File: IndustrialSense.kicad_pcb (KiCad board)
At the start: 6 copper layers, 0 parts

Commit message: [PCB/SCH][Added] Preliminary version
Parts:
- added C1: 47uF, easyeda2kicad:CAP-SMD_BD6.3-L6.6-W6.6-LS7.6-FD, F.Cu at (92.0, 112.7)
- added C12: 100n, Capacitor_SMD:C_0603_1608Metric, F.Cu at (105.7, 87.9)
- added C13: 22u, Capacitor_SMD:C_0805_2012Metric, F.Cu at (122.6, 93.0)
- added C14: 10u, Capacitor_SMD:C_1210_3225Metric, F.Cu at (120.5, 98.1)
- added C15: 100n, Capacitor_SMD:C_0402_1005Metric, F.Cu at (117.0, 96.9)
- added C16: 3.3n, Capacitor_SMD:C_0603_1608Metric, F.Cu at (115.0, 94.4)
- added C17: 100n, Capacitor_SMD:C_0402_1005Metric, F.Cu at (101.1, 121.6)
- added C18: 100n, Capacitor_SMD:C_0402_1005Metric, F.Cu at (89.8, 119.0)
- added C19: 100n, Capacitor_SMD:C_0402_1005Metric, F.Cu at (114.8, 112.4)
- added C20: 100n, Capacitor_SMD:C_0402_1005Metric, F.Cu at (112.3, 106.3)
- added C21: 10u, Capacitor_SMD:C_1210_3225Metric, F.Cu at (90.8, 107.3)
- added C22: 100n, Capacitor_SMD:C_0402_1005Metric, F.Cu at (90.7, 104.8)
- added C23: 10u, Capacitor_SMD:C_1210_3225Metric, F.Cu at (125.0, 123.8)
- added C24: 100n, Capacitor_SMD:C_0402_1005Metric, F.Cu at (95.4, 106.3)
- added C25: 220n, Capacitor_SMD:C_0402_1005Metric, F.Cu at (103.4, 107.2)
- added C26: 100n, Capacitor_SMD:C_0603_1608Metric, F.Cu at (104.2, 87.9)
- added C37: 1u, Capacitor_SMD:C_0402_1005Metric, F.Cu at (112.6, 122.1)
- added C38: 1u, Capacitor_SMD:C_0402_1005Metric, F.Cu at (135.1, 122.2)
- added C39: 1u, Capacitor_SMD:C_0402_1005Metric, F.Cu at (131.3, 122.2)
- added C4: 100u, Capacitor_SMD:C_1210_3225Metric, F.Cu at (117.5, 105.1)
- added C40: 100n, Capacitor_SMD:C_0603_1608Metric, F.Cu at (97.3, 58.3)
- added C41: 10u, Capacitor_SMD:C_0603_1608Metric, F.Cu at (95.8, 58.3)
- added C42: 10u, Capacitor_SMD:C_0603_1608Metric, F.Cu at (145.3, 64.3)
- added C43: 100n, Capacitor_SMD:C_0603_1608Metric, F.Cu at (143.8, 64.3)
- added C44: 100n, Capacitor_SMD:C_0402_1005Metric, F.Cu at (132.6, 83.4)
- added C45: 10u, Capacitor_SMD:C_0402_1005Metric, F.Cu at (133.6, 83.4)
- added C46: 1u, Capacitor_SMD:C_0603_1608Metric, F.Cu at (123.1, 82.5)
- added C47: 1u, Capacitor_SMD:C_0603_1608Metric, F.Cu at (118.9, 85.7)
- added C48: 100n, Capacitor_SMD:C_0603_1608Metric, F.Cu at (123.1, 84.0)
- added C5: 100n, Capacitor_SMD:C_0402_1005Metric, F.Cu at (130.1, 124.3)
- added C6: 100u, Capacitor_SMD:C_1210_3225Metric, F.Cu at (117.5, 101.8)
- added C7: 10u, easyeda2kicad:CAP-SMD_BD6.3-L6.6-W6.6-LS7.6-FD, F.Cu at (124.6, 116.6)
- added CN1: BM04B-SRSS-TB(LF)(SN), easyeda2kicad:CONN-SMD_BM04B-SRSS-TB, F.Cu at (92.3, 74.5)
- added CN2: B4B-ZR (LF)(SN), easyeda2kicad:CONN-TH_B4B-ZR-LF-SN, F.Cu at (92.1, 83.0)
- added CN3: ZH1.5-6P-LT, easyeda2kicad:CONN-SMD_ZH1.5-6P-LT, F.Cu at (125.8, 130.6)
- added Card1: XKTF-0803-0, easyeda2kicad:TF-SMD_XKTF-0803-0, F.Cu at (141.4, 84.6)
- added D1: SS24, Diode_SMD:D_SMA, F.Cu at (97.1, 90.2)
- added D10: CDSOT23-SM712, easyeda2kicad:SOT-23_L2.9-W1.3-P1.90-LS2.4-BR, F.Cu at (96.4, 83.1)
- added D16: WHITE2, LED_SMD:LED_0603_1608Metric, F.Cu at (98.3, 110.5)
- added D2: SS24, Diode_SMD:D_SMA, F.Cu at (91.6, 92.1)
- added D3: PESD0402-140, easyeda2kicad:D0402-BI, F.Cu at (143.4, 68.6)
- added D4: BV24C, easyeda2kicad:SOD-323_L1.7-W1.3-LS2.6-BI, F.Cu at (110.7, 123.6)
- added D5: DT1042-04SO-7, easyeda2kicad:SOT-26_L3.0-W1.6-P0.95-LS2.8-BL, F.Cu at (106.3, 121.7)
- added D6: 1N5819WS, Diode_SMD:D_SOD-323, F.Cu at (129.7, 88.5)
- added D7: 1N5819WS, Diode_SMD:D_SOD-323, F.Cu at (129.7, 91.4)
- added D8: 1N5819WS, Diode_SMD:D_SOD-323, F.Cu at (129.7, 94.3)
- added J2: Conn_02x05_Odd_Even, Connector_PinHeader_2.54mm:PinHeader_2x05_P2.54mm_Horizontal, F.Cu at (140.2, 120.6)
- added L2: RA-01SH, easyeda2kicad:WIRELM-SMD_RA-01SH, F.Cu at (132.5, 62.1)
- added L3: XAL6060-223MEC, easyeda2kicad:IND-SMD_L6.6-W6.4, F.Cu at (97.3, 96.3)
- added Q1: SISA14DN-T1-GE3, easyeda2kicad:POWERPAK-1212-8_L3.3-W3.1-P0.65-BL-EP, F.Cu at (95.7, 118.9)
- added Q13: MMBT3904, Package_TO_SOT_SMD:SOT-23, F.Cu at (142.0, 101.8)
- added Q15: LMBT3904DW1T1G, easyeda2kicad:SOT-363_L2.0-W1.3-P0.65-LS2.1-BR, F.Cu at (118.1, 78.1)
- added Q2: SISA14DN-T1-GE3, easyeda2kicad:POWERPAK-1212-8_L3.3-W3.1-P0.65-BL-EP, F.Cu at (101.1, 115.5)
- added Q3: SISA14DN-T1-GE3, easyeda2kicad:POWERPAK-1212-8_L3.3-W3.1-P0.65-BL-EP, F.Cu at (118.0, 111.0)
- added Q4: SISA14DN-T1-GE3, easyeda2kicad:POWERPAK-1212-8_L3.3-W3.1-P0.65-BL-EP, F.Cu at (113.7, 109.2)
- added Q5: CEM4435A, easyeda2kicad:SO-8_L4.9-W3.9-P1.27-LS5.9-BL, F.Cu at (91.0, 99.9)
- added Q6: CH221K, easyeda2kicad:SOT-23-6_L2.9-W1.6-P0.95-LS2.8-BL-2, F.Cu at (113.1, 119.3)
- added R1: 1M, Resistor_SMD:R_0402_1005Metric, F.Cu at (96.2, 121.7)
- added R10: 100k, Resistor_SMD:R_0402_1005Metric, F.Cu at (100.4, 110.5)
- added R11: 1k, Resistor_SMD:R_0402_1005Metric, F.Cu at (95.4, 107.3)
- added R12: 470k, Resistor_SMD:R_0402_1005Metric, F.Cu at (103.4, 104.5)
- added R13: 78.7k, Resistor_SMD:R_0402_1005Metric, F.Cu at (103.4, 105.5)
- added R18: 10k, Resistor_SMD:R_0402_1005Metric, F.Cu at (110.8, 87.2)
- added R19: 10k, Resistor_SMD:R_0402_1005Metric, F.Cu at (113.1, 83.2)
- added R2: 1M, Resistor_SMD:R_0402_1005Metric, F.Cu at (104.0, 116.0)
- added R3: 1M, Resistor_SMD:R_0402_1005Metric, F.Cu at (118.3, 113.8)
- added R4: 5.1k, Resistor_SMD:R_0402_1005Metric, F.Cu at (100.2, 126.0)
- added R47: 47k, Resistor_SMD:R_0603_1608Metric, F.Cu at (142.2, 98.9)
- added R48: 47k, Resistor_SMD:R_0603_1608Metric, F.Cu at (144.9, 99.7)
- added R49: 100k, Resistor_SMD:R_0603_1608Metric, F.Cu at (141.2, 105.0)
- added R5: 5.1k, Resistor_SMD:R_0402_1005Metric, F.Cu at (112.4, 126.2)
- added R50: 100k, Resistor_SMD:R_0603_1608Metric, F.Cu at (135.9, 86.3)
- added R53: 10k, Resistor_SMD:R_0603_1608Metric, F.Cu at (120.5, 77.9)
- added R54: 10k, Resistor_SMD:R_0603_1608Metric, F.Cu at (115.7, 77.9)
- added R55: 150k, Resistor_SMD:R_0603_1608Metric, F.Cu at (125.9, 91.3)
- added R56: 100k, Resistor_SMD:R_0603_1608Metric, F.Cu at (125.9, 89.8)
- added R57: 10k, Resistor_SMD:R_0603_1608Metric, F.Cu at (105.6, 76.6)
- added R58: 10k, Resistor_SMD:R_0603_1608Metric, F.Cu at (98.1, 69.0)
- added R59: 47k, Resistor_SMD:R_0402_1005Metric, F.Cu at (110.6, 118.7)
- added R6: 1M, Resistor_SMD:R_0402_1005Metric, F.Cu at (110.2, 109.5)
- added R60: 1k, Resistor_SMD:R_0402_1005Metric, F.Cu at (110.1, 120.5)
- added R67: 10, Resistor_SMD:R_0603_1608Metric, F.Cu at (101.9, 83.9)
- added R68: 10, Resistor_SMD:R_0603_1608Metric, F.Cu at (101.9, 82.4)
- added R69: 120, Resistor_SMD:R_0603_1608Metric, F.Cu at (99.4, 83.1)
- added R7: 120, Resistor_SMD:R_0402_1005Metric, F.Cu at (103.4, 108.2)
- added R8: 50m, easyeda2kicad:RES-SMD_L6.4-W3.2-R2512, F.Cu at (105.1, 99.5)
- added R9: 820k, Resistor_SMD:R_0402_1005Metric, F.Cu at (95.9, 104.8)
- added RF1: CONUFL001-SMD-T, easyeda2kicad:IPEX-SMD_3P-L2.6-W2.6-LS3.0, F.Cu at (146.4, 69.1)
- added SW2: SKRKAEE020, easyeda2kicad:SW-SMD_L3.9-W3.0-P4.45, F.Cu at (142.8, 108.5)
- added SW3: SKRKAEE020, easyeda2kicad:SW-SMD_L3.9-W3.0-P4.45, F.Cu at (96.0, 55.0)
- added U1: ESP32-S3-WROOM-1U-N16, easyeda2kicad:WIRELM-SMD_ESP32-S3-WROOM-1U, F.Cu at (110.0, 63.9)
- added U10: LM74700QDBVRQ1, easyeda2kicad:SOT-23-6_L2.9-W1.6-P0.95-LS2.8-BL, F.Cu at (109.8, 106.4)
- added U11: CN3795, easyeda2kicad:SSOP-10_L4.9-W3.9-P1.00-LS6.0-BL, F.Cu at (99.4, 105.4)
- added U12: XFL4020-222MEC_C122469, easyeda2kicad:IND-SMD_L4.0-W4.0_XAL4030-332MEC, F.Cu at (119.2, 89.2)
- added U14: CH334F, easyeda2kicad:QFN-24_L4.0-W4.0-P0.50-BL-EP2.8, F.Cu at (129.1, 82.7)
- added U15: TPS3831G33DQNR, easyeda2kicad:X2SON-4_L1.0-W1.0-P0.65-TL-EP, F.Cu at (99.2, 57.2)
- added U17: THVD1406DR, easyeda2kicad:SOIC-8_L4.9-W3.9-P1.27-LS6.0-BL, F.Cu at (108.3, 83.2)
- added U2: B5B-ZR-(LF)(SN), easyeda2kicad:CONN-TH_5P-P1.50_B5B-ZR-LF-SN, F.Cu at (92.2, 64.6)
- added U3: CH343P, easyeda2kicad:TQFN-16_L3.0-W3.0-P0.50-BL-EP1.7, F.Cu at (118.9, 82.3)
- added U4: MAX17049G+T10, easyeda2kicad:WSON-8_L2.0-W2.0-P0.50-BL-EP0.9, F.Cu at (132.1, 120.0)
- added U5: LM74700QDBVRQ1, easyeda2kicad:SOT-23-6_L2.9-W1.6-P0.95-LS2.8-BL, F.Cu at (92.1, 119.1)
- added U6: LM74700QDBVRQ1, easyeda2kicad:SOT-23-6_L2.9-W1.6-P0.95-LS2.8-BL, F.Cu at (101.2, 119.2)
- added U7: TPS62132RGTT, easyeda2kicad:VQFN-16_L3.0-W3.0-P0.50-TL-EP, F.Cu at (118.2, 93.8)
- added U8: LM74700QDBVRQ1, easyeda2kicad:SOT-23-6_L2.9-W1.6-P0.95-LS2.8-BL, F.Cu at (114.7, 114.7)
- added U9: XC6209F332MR-G, easyeda2kicad:SOT-25-5_L3.0-W1.8-P0.95-LS3.0-BR, F.Cu at (133.2, 124.8)
- added USB1: TYPE-C 16PIN 2MD(073), easyeda2kicad:USB-C-SMD_TYPE-C-6PIN-2MD-073, F.Cu at (106.3, 128.7)
- added X1: X322512MSB4SI, easyeda2kicad:CRYSTAL-SMD_4P-L3.2-W2.5-BL, F.Cu at (128.3, 76.9)
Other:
- board outline added: 62 x 83 mm
- rule pad_to_mask_clearance: 0.05 -> 0.1
- board text removed: "30°"
- board text removed: "3× 120°"

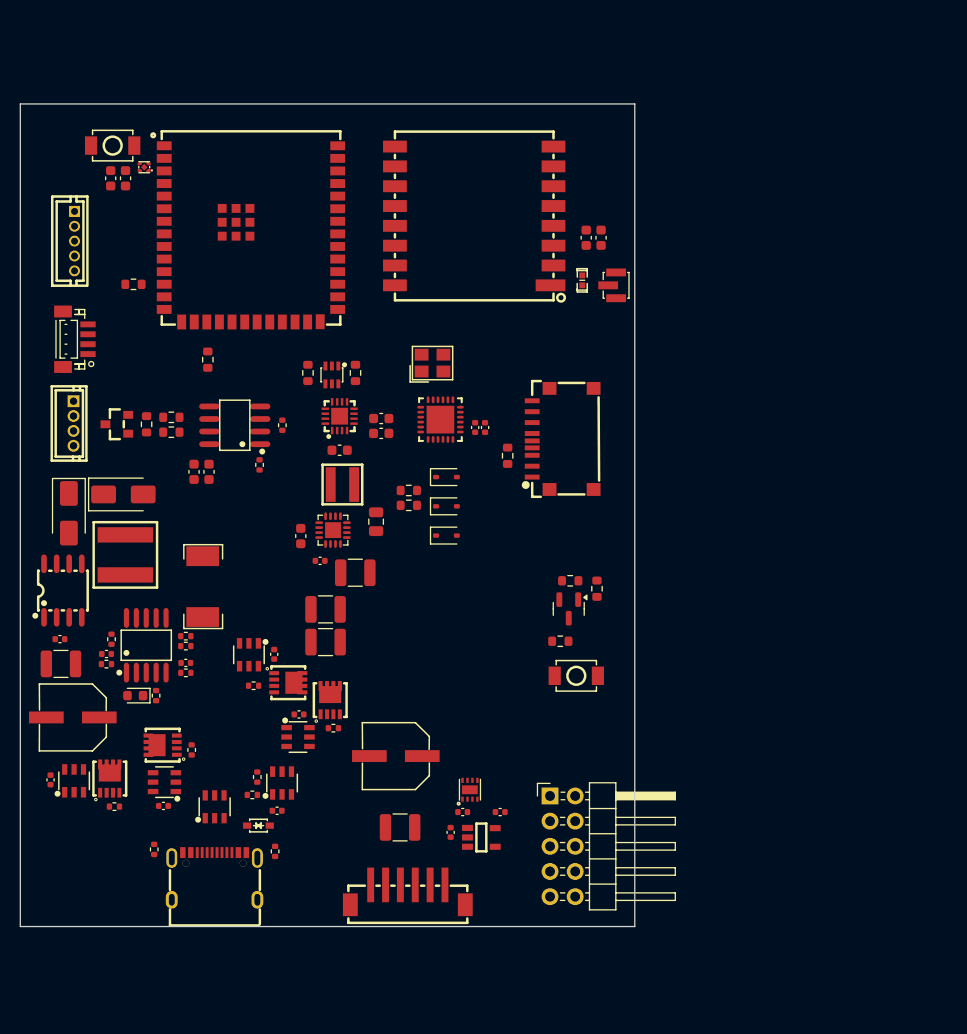
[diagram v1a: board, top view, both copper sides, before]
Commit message: [Schematic][Added] Connectors and first PCB layout
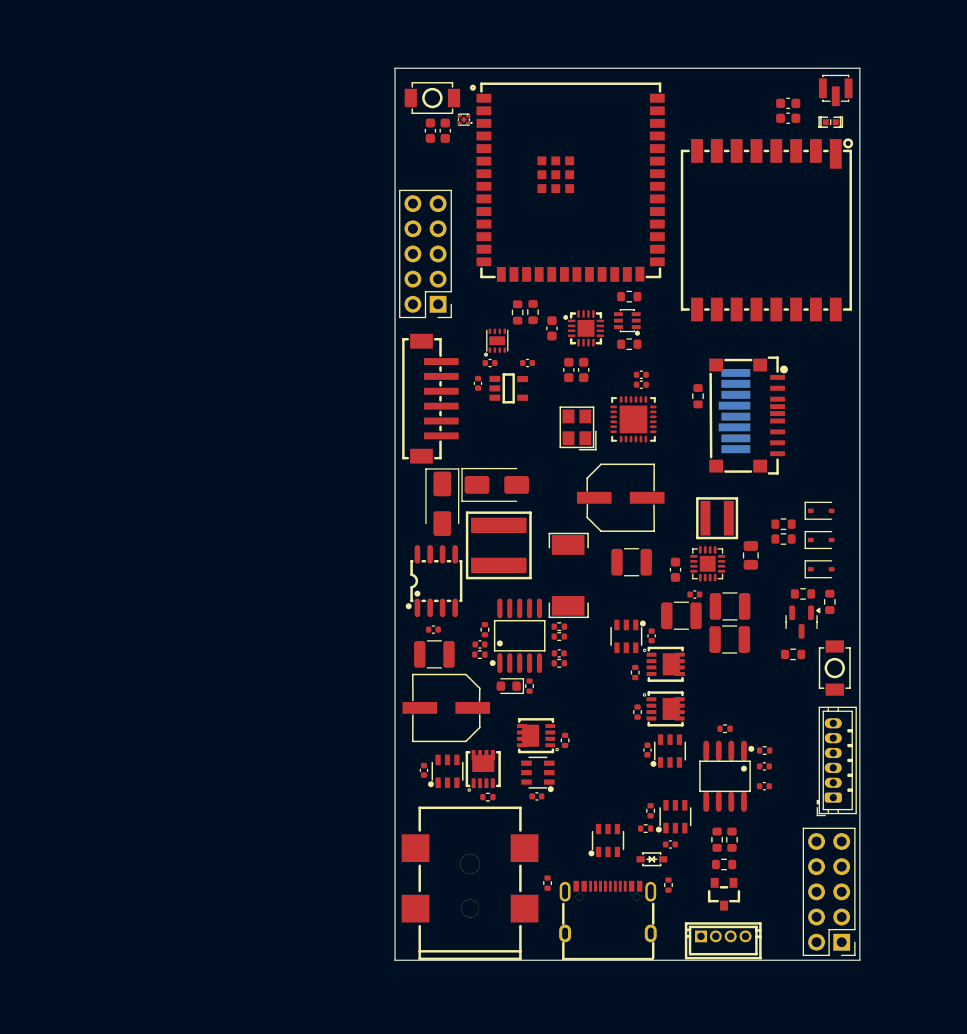
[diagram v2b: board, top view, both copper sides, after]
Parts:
- removed CN1: BM04B-SRSS-TB(LF)(SN), easyeda2kicad:CONN-SMD_BM04B-SRSS-TB
- removed J2: Conn_02x05_Odd_Even, Connector_PinHeader_2.54mm:PinHeader_2x05_P2.54mm_Horizontal
- removed U2: B5B-ZR-(LF)(SN), easyeda2kicad:CONN-TH_5P-P1.50_B5B-ZR-LF-SN
- added DC1: DC-005-5A-2.0-SMT, easyeda2kicad:DC-IN-TH_DC-005-5A-2.0-SMT, F.Cu at (132.1, 128.9)
- added J1: Conn_01x06_Socket, Connector_JST:JST_ZH_B6B-ZR_1x06_P1.50mm_Vertical, F.Cu at (168.7, 120.8)
- added J3: Conn_02x05_Odd_Even, Connector_PinHeader_2.54mm:PinHeader_2x05_P2.54mm_Vertical, F.Cu at (128.9, 71.0)
- added J3: Conn_02x05_Odd_Even, Connector_PinHeader_2.54mm:PinHeader_2x05_P2.54mm_Vertical, F.Cu at (169.6, 135.4)
- added REF**: Micro_SD_Card, Library:microSD_card, B.Cu at (165.1, 81.8)
- C12, C26: footprint Capacitor_SMD:C_0603_1608Metric -> Capacitor_SMD:C_0402_1005Metric
- moved CN2 83.5 mm to (157.6, 134.8), turned to 180 degrees
- moved D10 77.5 mm to (157.7, 130.5), turned to 90 degrees
- moved R69 73.3 mm to (157.7, 127.5), turned to 180 degrees
- moved R67 69.9 mm to (158.5, 125.0), turned to -90 degrees
- moved R68 69.6 mm to (157.0, 125.0), turned to -90 degrees
- moved C26 65.7 mm to (161.8, 119.6), turned to 0 degrees
- moved C12 63.4 mm to (161.8, 117.6), turned to 0 degrees
- moved U17 60.8 mm to (157.8, 118.6), turned to 180 degrees
- moved R18 58.6 mm to (161.8, 116.0), turned to 180 degrees
- moved R19 54.2 mm to (157.8, 113.8), turned to 180 degrees
- moved CN3 50.1 mm to (128.2, 80.5), turned to -90 degrees
- moved C38 45.4 mm to (137.9, 76.9)
- moved C39 45.4 mm to (134.1, 76.9)
- moved C5 45.4 mm to (132.9, 79.0)
- moved U4 45.4 mm to (134.8, 74.7)
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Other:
- board size 62 x 83 mm -> 46.9 x 90 mm

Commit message: [Schematic/PCB][Added] Connectors, layout, preliminar routing
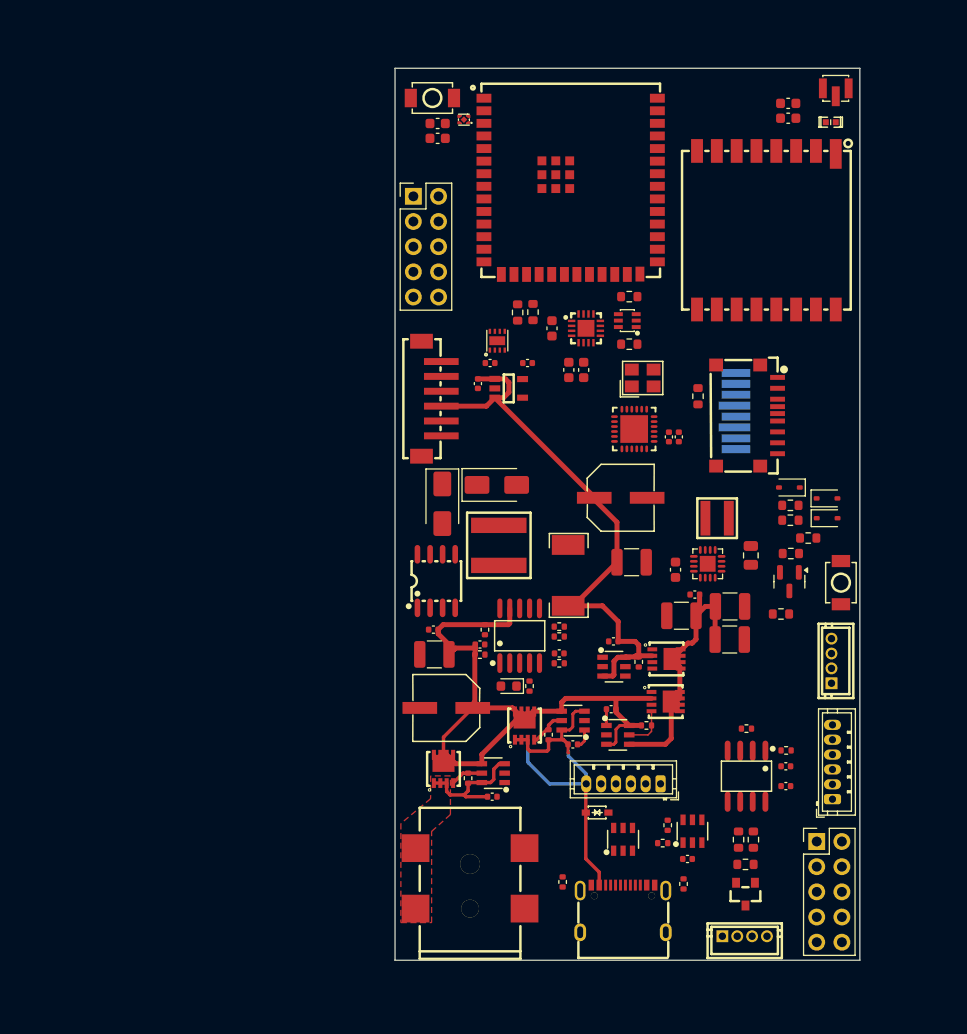
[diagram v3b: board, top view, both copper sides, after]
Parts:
- removed the J3 at (128.9, 71.0)
- removed the J3 at (169.6, 135.4)
- added CN4: B4B-ZR (LF)(SN), easyeda2kicad:CONN-TH_B4B-ZR-LF-SN, F.Cu at (168.6, 107.0)
- added J3: Conn_01x06_Socket, Connector_JST:JST_ZH_B6B-ZR_1x06_P1.50mm_Vertical, F.Cu at (168.7, 121.0)
- added J5: Conn_01x10_Socket, Connector_PinHeader_2.54mm:PinHeader_2x05_P2.54mm_Vertical, F.Cu at (167.1, 125.2)
- added J6: Conn_01x10_Socket, Connector_PinHeader_2.54mm:PinHeader_2x05_P2.54mm_Vertical, F.Cu at (126.4, 60.1)
- moved J1 17.5 mm to (151.3, 119.4), turned to 180 degrees
- moved SW2 8.64 mm to (169.5, 99.1)
- moved X1 8.29 mm to (149.5, 78.5), turned to 0 degrees
- moved C18 7.39 mm to (134.3, 120.7), turned to 180 degrees
- moved C45 7.32 mm to (153.1, 84.4), turned to 90 degrees
- moved D4 7.26 mm to (144.9, 122.3)
- moved R48 6.80 mm to (166.2, 94.6), turned to 180 degrees
- moved C17 6.38 mm to (142.4, 115.4)
- moved U6 6.34 mm to (142.5, 113.0)
- moved C44 5.96 mm to (152.1, 84.4), turned to 90 degrees
- moved U8 5.51 mm to (147.0, 114.5), turned to -90 degrees
- moved C19 5.51 mm to (146.3, 111.9), turned to 0 degrees
- moved D8 5.18 mm to (168.1, 92.6)
- moved U5 4.62 mm to (134.4, 118.3), turned to 90 degrees
- moved R47 4.26 mm to (164.4, 96.2)
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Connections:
- CN2 pad 1: V_MAIN -> GND
- CN2 pad 4: GND -> V_MAIN
- D5 pad 1: /Project Architecture/HUB/USBCD+ -> /Project Architecture/External Connectors/USBCD-
- D5 pad 3: /Project Architecture/HUB/USBCD- -> /Project Architecture/External Connectors/USBCD+
- DC1 pad 1: unconnected-(DC1-Pad1) -> VSUN
- DC1 pad 2: unconnected-(DC1-Pad2) -> GND
- DC1 pad 3: unconnected-(DC1-Pad3) -> GND
- J1 pad 1: unconnected-(J1-Pin_1-Pad1) -> GND
- J1 pad 2: unconnected-(J1-Pin_2-Pad2) -> /Project Architecture/External Connectors/CC2
- J1 pad 3: unconnected-(J1-Pin_3-Pad3) -> /Project Architecture/External Connectors/USBCD+
- J1 pad 4: unconnected-(J1-Pin_4-Pad4) -> /Project Architecture/External Connectors/USBCD-
- J1 pad 5: unconnected-(J1-Pin_5-Pad5) -> /Project Architecture/External Connectors/CC1
- J1 pad 6: unconnected-(J1-Pin_6-Pad6) -> VBUS
- Q6 pad 4: /Project Architecture/Power Management/USBCC1 -> /Project Architecture/External Connectors/CC1
- Q6 pad 5: /Project Architecture/Power Management/USBCC2 -> /Project Architecture/External Connectors/CC2
- R4 pad 1: /Project Architecture/Power Management/USBCC1 -> /Project Architecture/External Connectors/CC1
- R5 pad 1: /Project Architecture/Power Management/USBCC2 -> /Project Architecture/External Connectors/CC2
- U1 pad 31: /Project Architecture/MCU/LOCK_PWR -> /Project Architecture/MCU/PWR_KEY
- U1 pad 32: /Project Architecture/External Connectors/LTE_ON -> /Project Architecture/MCU/LOCK_PWR
- U1 pad 33: /Project Architecture/External Connectors/LTE_RST -> /Project Architecture/External Connectors/GPIO40B
- U1 pad 34: /Project Architecture/External Connectors/LTE_RXD2 -> /Project Architecture/External Connectors/GPIO41G
- U1 pad 35: /Project Architecture/External Connectors/LTE_TXD2 -> /Project Architecture/External Connectors/GPIO42R
- U1 pad 4: /Project Architecture/External Connectors/GPIO4 -> /Project Architecture/External Connectors/LTE_TXD2
- U1 pad 5: /Project Architecture/External Connectors/GPIO5 -> /Project Architecture/External Connectors/LTE_RXD2
- U1 pad 6: /Project Architecture/External Connectors/GPIO6 -> /Project Architecture/External Connectors/LTE_RST
- U1 pad 7: /Project Architecture/External Connectors/GPIO7 -> /Project Architecture/External Connectors/LTE_ON
- U1 pad 8: /Project Architecture/External Connectors/GPIO8 -> /Project Architecture/External Connectors/GPIO15
- U1 pad 9: /Project Architecture/MCU/PWR_KEY -> /Project Architecture/External Connectors/GPIO16
- U14 pad 10: /Project Architecture/HUB/CH343_USBD- -> /Project Architecture/HUB/ESP_USBD+
- U14 pad 11: /Project Architecture/HUB/ESP_USBD- -> /Project Architecture/External Connectors/LTE_USBD-
- U14 pad 12: /Project Architecture/HUB/ESP_USBD+ -> /Project Architecture/External Connectors/LTE_USBD+
- U14 pad 14: /Project Architecture/HUB/USBCD- -> /Project Architecture/External Connectors/USBCD-
- U14 pad 15: /Project Architecture/HUB/USBCD+ -> /Project Architecture/External Connectors/USBCD+
- U14 pad 7: /Project Architecture/External Connectors/LTE_USBD- -> /Project Architecture/HUB/CH343_USBD+
- U14 pad 8: /Project Architecture/External Connectors/LTE_USBD+ -> /Project Architecture/HUB/CH343_USBD-
- U14 pad 9: /Project Architecture/HUB/CH343_USBD+ -> /Project Architecture/HUB/ESP_USBD-
- USB1 pad 10: /Project Architecture/Power Management/USBCC2 -> /Project Architecture/External Connectors/CC2
- USB1 pad 4: /Project Architecture/Power Management/USBCC1 -> /Project Architecture/External Connectors/CC1
- USB1 pad 5: /Project Architecture/HUB/USBCD- -> /Project Architecture/External Connectors/USBCD-
- USB1 pad 6: /Project Architecture/HUB/USBCD+ -> /Project Architecture/External Connectors/USBCD+
- USB1 pad 7: /Project Architecture/HUB/USBCD- -> /Project Architecture/External Connectors/USBCD-
- USB1 pad 8: /Project Architecture/HUB/USBCD+ -> /Project Architecture/External Connectors/USBCD+
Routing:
- net V_CHRG: track 0.00 -> 66.8 mm
- net V_BAT: track 0.00 -> 58.3 mm
- net VBUS: track 0.00 -> 37.1 mm
- net V_MAIN: track 0.00 -> 26.1 mm
- net VSUN: track 0.00 -> 12.9 mm
- net Net-(Q3-G): track 0.00 -> 4.43 mm
- net Net-(Q2-G): track 0.00 -> 3.84 mm
- net Net-(Q1-G): track 0.00 -> 3.31 mm
- net Net-(U6-VCAP): track 0.00 -> 1.94 mm
- net Net-(U8-VCAP): track 0.00 -> 1.64 mm
- added copper zone on F.Cu, net VSUN
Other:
- copper layers 6 -> 4
